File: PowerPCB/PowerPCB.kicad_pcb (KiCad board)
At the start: 2 copper layers, 140 x 70 mm, 60 parts, among them J1 Conn_01x03_Male, J2 Conn_01x10_Male, J3 Conn_01x07_Male, K1 1721081-5, K2 1721081-5, K3 1721081-5, Q1 Q_PMOS_DGS, U1 NCP1117-5.0_SOT223, U2 NCP1117-3.3_SOT223, U3 MCP2562-E-P, U4 MCP2562-E-P, U5 STM32F413ZHTx

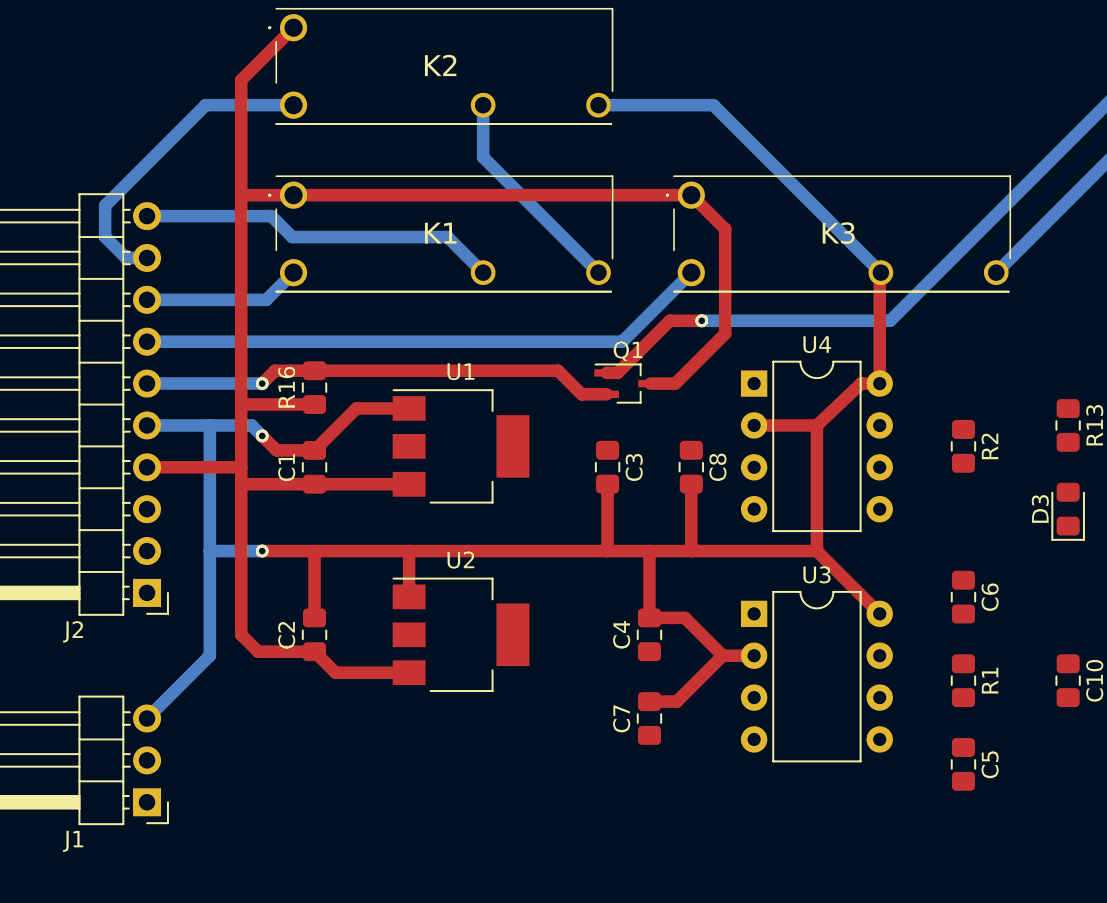
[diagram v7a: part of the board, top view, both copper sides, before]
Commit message: Routed linear regulators and most of the CAN transceivers
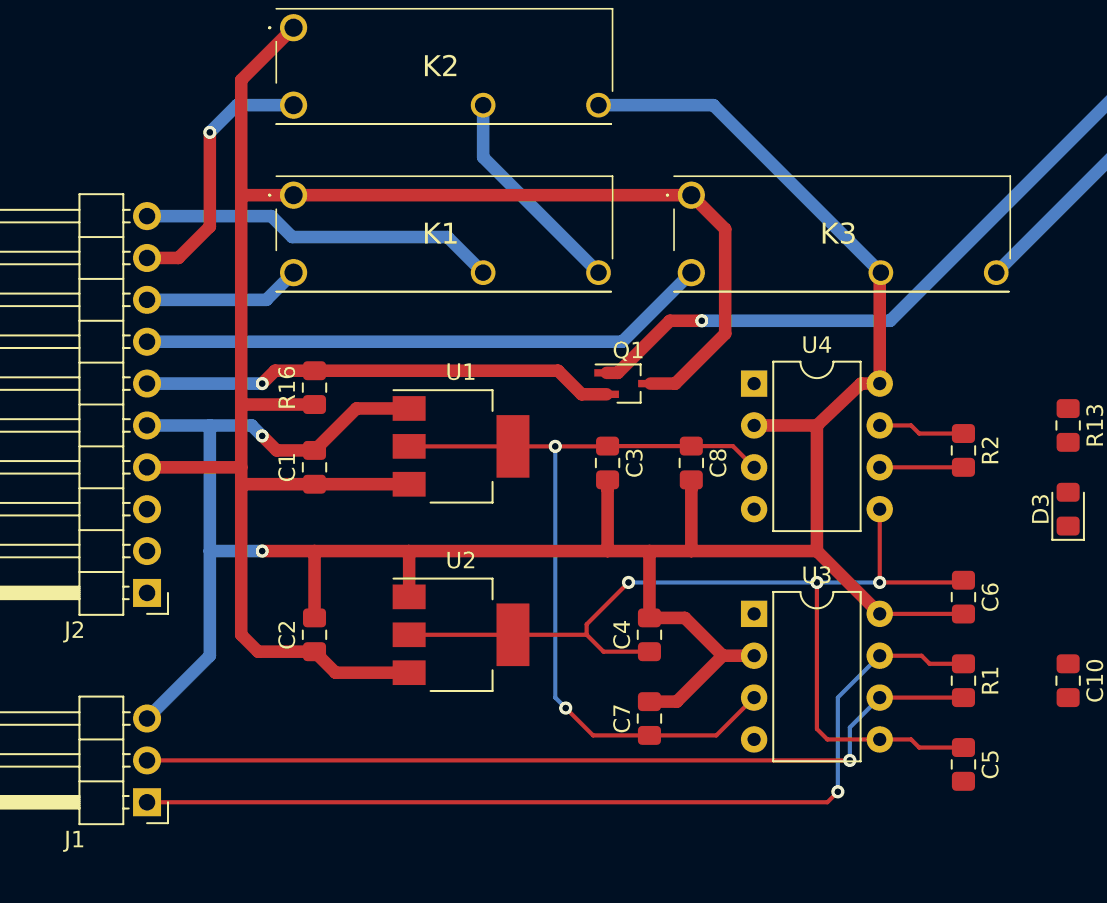
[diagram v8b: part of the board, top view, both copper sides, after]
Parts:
- moved C3 0.25 mm to (82.5, 73.4)
- moved C8 0.25 mm to (87.6, 73.4)
- moved R2 0.25 mm to (104.1, 72.6)
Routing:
- net VCC_3.3: track 0.00 -> 62.3 mm, vias 0 -> 3
- net BMS_CAN_HI: track 0.00 -> 56.8 mm, vias 0 -> 1
- net BMS_CAN_LO: track 0.00 -> 52.3 mm, vias 0 -> 1
- net VCC_5: track 0.00 -> 50.7 mm, vias 0 -> 2
- net GND: track 155.4 -> 161.0 mm
- net MAIN_CAN_HI: track 0.00 -> 5.28 mm
- net MAIN_CAN_LO: track 0.00 -> 5.08 mm
- net Net-(J2-Pad9): track 18.9 -> 16.1 mm, vias 0 -> 1
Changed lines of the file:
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@@
     (thickness 1.6)
     (drawings 4)
-    (tracks 89)
+    (tracks 145)
     (zones 0)
     (modules 60)
@@
     (via_min_size 0.4)
     (via_min_drill 0.3)
+    (user_via 1.524 0.762)
     (uvia_size 0.3)
     (uvia_drill 0.1)
@@
     )
   )
-  (module Resistor_SMD:R_0805_2012Metric_Pad1.15x1.40mm_HandSolder locked (layer F.Cu)
-    (at 104.14 72.39 270)
+  (module Resistor_SMD:R_0805_2012Metric_Pad1.15x1.40mm_HandSolder (layer F.Cu)
+    (at 104.14 72.635 270)
     (descr "Resistor SMD 0805 (2012 Metric), square (rectangular) end terminal, IPC_7351 nominal with elongated pad for handsoldering. (Body size source: https://docs.google.com/spreadsheets/d/1BsfQQcO9C6DZCsRaXUlFlo91Tg2WpOkGARC1WS5S8t0/edit?usp=sharing), generated with kicad-footprint-generator")
     (tags "resistor handsolder")
@@
     )
   )
-  (module Capacitor_SMD:C_0805_2012Metric_Pad1.15x1.40mm_HandSolder locked (layer F.Cu)
-    (at 87.63 73.651 270)
+  (module Capacitor_SMD:C_0805_2012Metric_Pad1.15x1.40mm_HandSolder (layer F.Cu)
+    (at 87.63 73.397 270)
     (descr "Capacitor SMD 0805 (2012 Metric), square (rectangular) end terminal, IPC_7351 nominal with elongated pad for handsoldering. (Body size source: https://docs.google.com/spreadsheets/d/1BsfQQcO9C6DZCsRaXUlFlo91Tg2WpOkGARC1WS5S8t0/edit?usp=sharing), generated with kicad-footprint-generator")
     (tags "capacitor handsolder")
@@
     )
   )
-  (module Capacitor_SMD:C_0805_2012Metric_Pad1.15x1.40mm_HandSolder locked (layer F.Cu)
-    (at 82.55 73.651 270)
+  (module Capacitor_SMD:C_0805_2012Metric_Pad1.15x1.40mm_HandSolder (layer F.Cu)
+    (at 82.55 73.397 270)
     (descr "Capacitor SMD 0805 (2012 Metric), square (rectangular) end terminal, IPC_7351 nominal with elongated pad for handsoldering. (Body size source: https://docs.google.com/spreadsheets/d/1BsfQQcO9C6DZCsRaXUlFlo91Tg2WpOkGARC1WS5S8t0/edit?usp=sharing), generated with kicad-footprint-generator")
     (tags "capacitor handsolder")
@@
   (segment (start 67.315 70.09) (end 70.51 70.09) (width 0.762) (layer F.Cu) (net 1))
   (segment (start 64.77 72.635) (end 67.315 70.09) (width 0.762) (layer F.Cu) (net 1))
-  (segment (start 82.55 75.251) (end 82.55 78.74) (width 0.762) (layer F.Cu) (net 1))
-  (segment (start 82.55 74.676) (end 82.55 75.251) (width 0.762) (layer F.Cu) (net 1))
   (segment (start 70.485 78.74) (end 82.55 78.74) (width 0.762) (layer F.Cu) (net 1))
-  (segment (start 87.63 74.676) (end 87.63 78.74) (width 0.762) (layer F.Cu) (net 1))
   (segment (start 87.63 78.74) (end 95.25 78.74) (width 0.762) (layer F.Cu) (net 1))
   (segment (start 95.25 71.25863) (end 95.25 78.74) (width 0.762) (layer F.Cu) (net 1))
@@
   (segment (start 99.06 61.92) (end 99.13 61.85) (width 0.762) (layer F.Cu) (net 1))
   (segment (start 99.06 68.58) (end 99.06 61.92) (width 0.762) (layer F.Cu) (net 1))
+  (segment (start 82.55 74.997) (end 82.55 78.74) (width 0.762) (layer F.Cu) (net 1))
+  (segment (start 82.55 74.422) (end 82.55 74.997) (width 0.762) (layer F.Cu) (net 1))
+  (segment (start 87.63 74.997) (end 87.63 78.74) (width 0.762) (layer F.Cu) (net 1))
+  (segment (start 87.63 74.422) (end 87.63 74.997) (width 0.762) (layer F.Cu) (net 1))
+  (segment (start 104.131 82.55) (end 104.14 82.559) (width 0.254) (layer F.Cu) (net 1))
+  (segment (start 99.06 82.55) (end 104.131 82.55) (width 0.254) (layer F.Cu) (net 1))
   (segment (start 70.505 74.685) (end 70.51 74.69) (width 0.762) (layer F.Cu) (net 2))
   (segment (start 64.77 74.685) (end 70.505 74.685) (width 0.762) (layer F.Cu) (net 2))
@@
   (segment (start 86.33 64.77) (end 88.265 64.77) (width 0.762) (layer F.Cu) (net 11))
   (segment (start 83.17 67.93) (end 86.33 64.77) (width 0.762) (layer F.Cu) (net 11))
+  (segment (start 70.51 83.82) (end 76.81 83.82) (width 0.254) (layer F.Cu) (net 12))
+  (segment (start 76.81 83.82) (end 81.28 83.82) (width 0.254) (layer F.Cu) (net 12))
+  (segment (start 82.305 84.845) (end 85.09 84.845) (width 0.254) (layer F.Cu) (net 12))
+  (segment (start 81.28 83.82) (end 82.305 84.845) (width 0.254) (layer F.Cu) (net 12))
+  (segment (start 81.28 83.82) (end 81.28 83.185) (width 0.254) (layer F.Cu) (net 12))
+  (via (at 83.82 80.645) (size 0.8) (drill 0.4) (layers F.Cu B.Cu) (net 12))
+  (segment (start 81.28 83.185) (end 83.82 80.645) (width 0.254) (layer F.Cu) (net 12))
+  (via (at 99.06 80.645) (size 0.8) (drill 0.4) (layers F.Cu B.Cu) (net 12))
+  (segment (start 99.06 80.645) (end 99.06 76.2) (width 0.254) (layer F.Cu) (net 12))
+  (segment (start 104.004 80.645) (end 104.14 80.509) (width 0.254) (layer F.Cu) (net 12))
+  (segment (start 99.06 80.645) (end 104.004 80.645) (width 0.254) (layer F.Cu) (net 12))
+  (segment (start 99.06 90.17) (end 95.885 90.17) (width 0.254) (layer F.Cu) (net 12))
+  (segment (start 95.885 90.17) (end 95.25 89.535) (width 0.254) (layer F.Cu) (net 12))
+  (segment (start 95.25 89.535) (end 95.25 80.645) (width 0.254) (layer F.Cu) (net 12))
+  (via (at 95.25 80.645) (size 0.8) (drill 0.4) (layers F.Cu B.Cu) (net 12))
+  (segment (start 83.82 80.645) (end 95.25 80.645) (width 0.254) (layer B.Cu) (net 12))
+  (segment (start 95.25 80.645) (end 99.06 80.645) (width 0.254) (layer B.Cu) (net 12))
+  (segment (start 99.06 90.17) (end 100.965 90.17) (width 0.254) (layer F.Cu) (net 12))
+  (segment (start 101.455 90.66) (end 104.14 90.66) (width 0.254) (layer F.Cu) (net 12))
+  (segment (start 100.965 90.17) (end 101.455 90.66) (width 0.254) (layer F.Cu) (net 12))
+  (segment (start 70.51 72.39) (end 76.81 72.39) (width 0.254) (layer F.Cu) (net 13))
+  (segment (start 82.532 72.39) (end 82.55 72.372) (width 0.254) (layer F.Cu) (net 13))
+  (segment (start 87.63 72.372) (end 82.55 72.372) (width 0.254) (layer F.Cu) (net 13))
+  (segment (start 90.152 72.372) (end 91.44 73.66) (width 0.254) (layer F.Cu) (net 13))
+  (segment (start 87.63 72.372) (end 90.152 72.372) (width 0.254) (layer F.Cu) (net 13))
+  (segment (start 89.145 89.925) (end 91.44 87.63) (width 0.254) (layer F.Cu) (net 13))
+  (segment (start 85.09 89.925) (end 89.145 89.925) (width 0.254) (layer F.Cu) (net 13))
+  (segment (start 85.09 89.925) (end 81.67 89.925) (width 0.254) (layer F.Cu) (net 13))
+  (via (at 80.01 88.265) (size 0.8) (drill 0.4) (layers F.Cu B.Cu) (net 13))
+  (segment (start 81.67 89.925) (end 80.01 88.265) (width 0.254) (layer F.Cu) (net 13))
+  (via (at 79.375 72.39) (size 0.8) (drill 0.4) (layers F.Cu B.Cu) (net 13))
+  (segment (start 79.375 87.63) (end 79.375 72.39) (width 0.254) (layer B.Cu) (net 13))
+  (segment (start 80.01 88.265) (end 79.375 87.63) (width 0.254) (layer B.Cu) (net 13))
+  (segment (start 76.81 72.39) (end 79.375 72.39) (width 0.254) (layer F.Cu) (net 13))
+  (segment (start 79.375 72.39) (end 82.532 72.39) (width 0.254) (layer F.Cu) (net 13))
+  (segment (start 99.06 87.63) (end 104.14 87.63) (width 0.254) (layer F.Cu) (net 14))
+  (via (at 97.247 91.44) (size 0.8) (drill 0.4) (layers F.Cu B.Cu) (net 14))
+  (segment (start 54.61 91.44) (end 97.247 91.44) (width 0.254) (layer F.Cu) (net 14))
+  (segment (start 97.247 89.443) (end 99.06 87.63) (width 0.254) (layer B.Cu) (net 14))
+  (segment (start 97.247 91.44) (end 97.247 89.443) (width 0.254) (layer B.Cu) (net 14))
+  (segment (start 104.14 85.58) (end 102.09 85.58) (width 0.254) (layer F.Cu) (net 15))
+  (segment (start 101.6 85.09) (end 99.06 85.09) (width 0.254) (layer F.Cu) (net 15))
+  (segment (start 102.09 85.58) (end 101.6 85.09) (width 0.254) (layer F.Cu) (net 15))
+  (segment (start 96.52 87.63) (end 99.06 85.09) (width 0.254) (layer B.Cu) (net 15))
+  (segment (start 96.52 93.345) (end 96.52 87.63) (width 0.254) (layer B.Cu) (net 15))
+  (via (at 96.52 93.345) (size 0.8) (drill 0.4) (layers F.Cu B.Cu) (net 15))
+  (segment (start 95.885 93.98) (end 96.52 93.345) (width 0.254) (layer F.Cu) (net 15))
+  (segment (start 54.61 93.98) (end 95.885 93.98) (width 0.254) (layer F.Cu) (net 15))
   (segment (start 75 61.85) (end 72.84 59.69) (width 0.762) (layer B.Cu) (net 16))
   (segment (start 63.420882 59.69) (end 62.150882 58.42) (width 0.762) (layer B.Cu) (net 16))
   (segment (start 72.84 59.69) (end 63.420882 59.69) (width 0.762) (layer B.Cu) (net 16))
   (segment (start 54.61 58.42) (end 62.150882 58.42) (width 0.762) (layer B.Cu) (net 16))
-  (segment (start 58.165 51.69) (end 63.5 51.69) (width 0.762) (layer B.Cu) (net 17))
-  (segment (start 52.07 59.69) (end 52.07 57.785) (width 0.762) (layer B.Cu) (net 17))
-  (segment (start 54.61 60.96) (end 53.34 60.96) (width 0.762) (layer B.Cu) (net 17))
-  (segment (start 52.07 57.785) (end 58.165 51.69) (width 0.762) (layer B.Cu) (net 17))
-  (segment (start 53.34 60.96) (end 52.07 59.69) (width 0.762) (layer B.Cu) (net 17))
+  (via (at 58.42 53.34) (size 0.8) (drill 0.4) (layers F.Cu B.Cu) (net 17))
+  (segment (start 54.61 60.96) (end 56.515 60.96) (width 0.762) (layer F.Cu) (net 17))
+  (segment (start 58.42 59.055) (end 58.42 53.34) (width 0.762) (layer F.Cu) (net 17))
+  (segment (start 56.515 60.96) (end 58.42 59.055) (width 0.762) (layer F.Cu) (net 17))
+  (segment (start 63.5 51.69) (end 60.07 51.69) (width 0.762) (layer B.Cu) (net 17))
+  (segment (start 60.07 51.69) (end 58.42 53.34) (width 0.762) (layer B.Cu) (net 17))
+  (segment (start 99.06 73.66) (end 104.14 73.66) (width 0.254) (layer F.Cu) (net 18))
+  (segment (start 104.14 71.61) (end 101.455 71.61) (width 0.254) (layer F.Cu) (net 19))
+  (segment (start 100.965 71.12) (end 99.06 71.12) (width 0.254) (layer F.Cu) (net 19))
+  (segment (start 101.455 71.61) (end 100.965 71.12) (width 0.254) (layer F.Cu) (net 19))
   (segment (start 75 54.85) (end 82 61.85) (width 0.762) (layer B.Cu) (net 20))
   (segment (start 75 51.69) (end 75 54.85) (width 0.762) (layer B.Cu) (net 20))
